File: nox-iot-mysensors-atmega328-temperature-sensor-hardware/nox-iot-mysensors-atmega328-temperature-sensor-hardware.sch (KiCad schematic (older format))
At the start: 14 parts, among them J1 Conn_01x02, J2 FTDI232, U1 ATmega328P-PU, U2 DHT11, U3 NRF24L01+, U5 LM317, Y1 16 MHZ

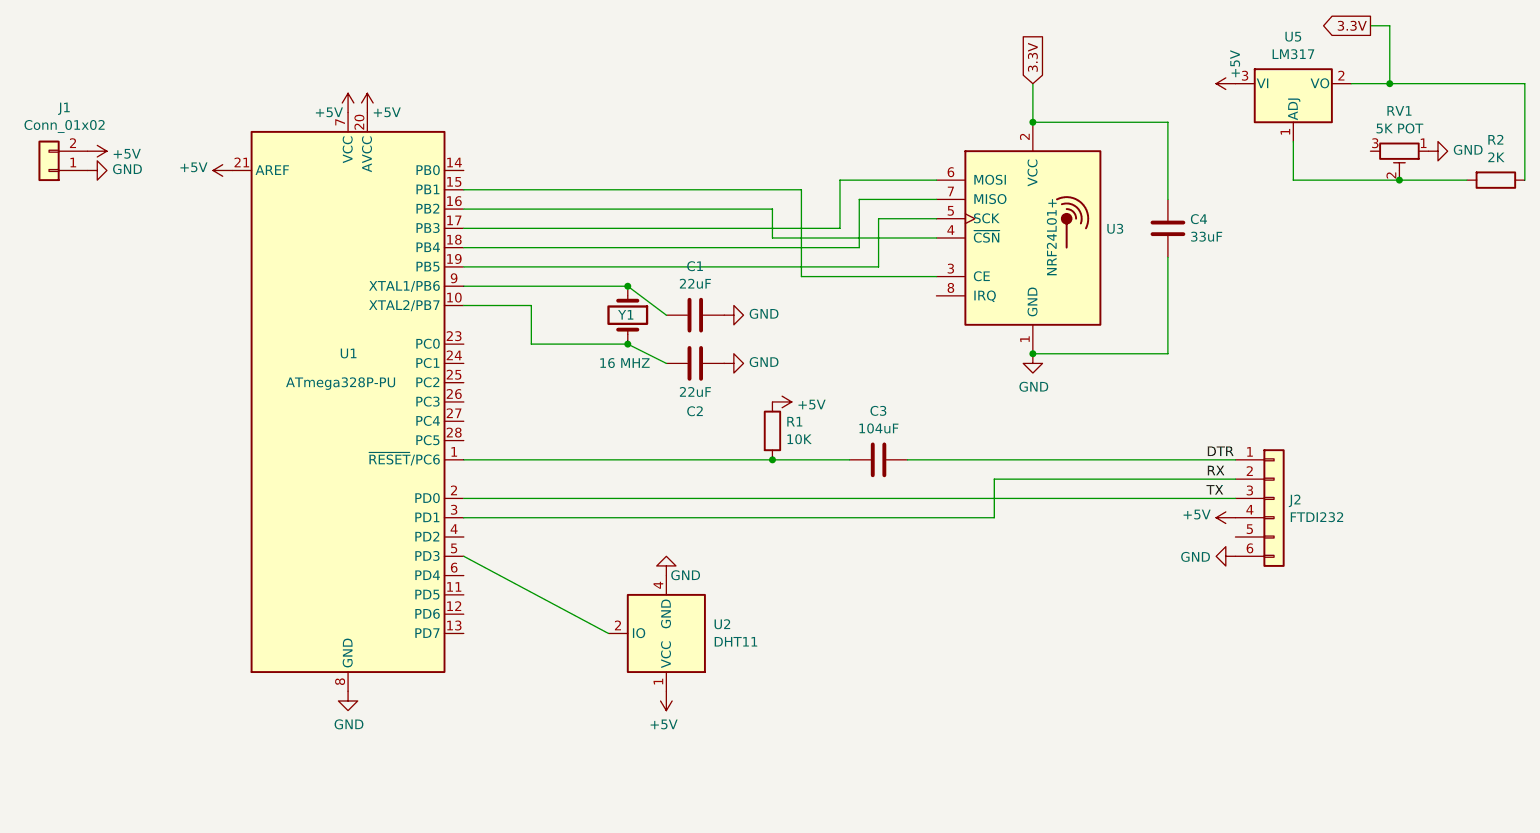
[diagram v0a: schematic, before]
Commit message: aht10 sensor instead of dht11 and 3.3v boost
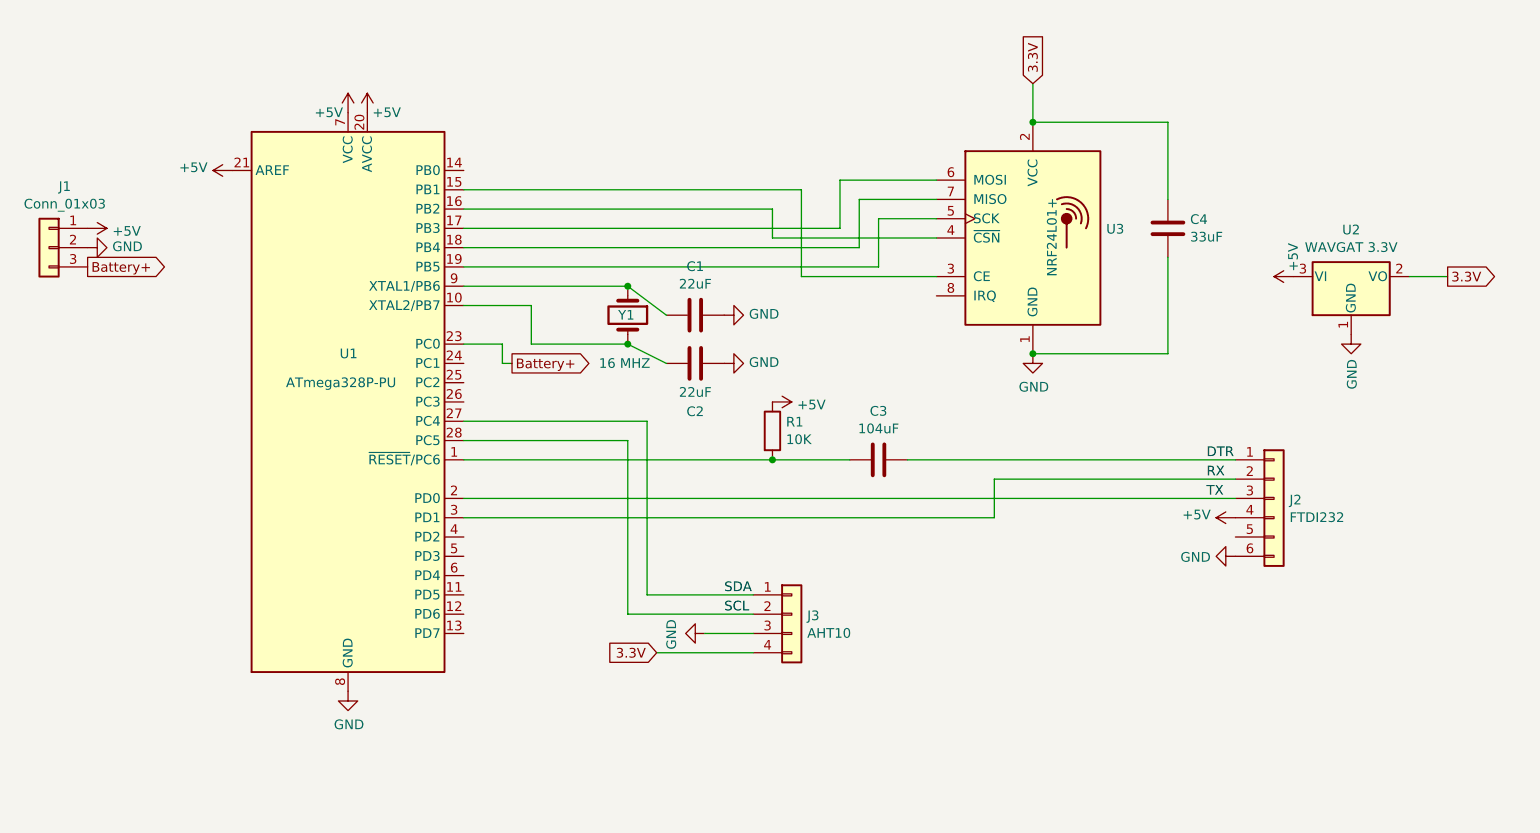
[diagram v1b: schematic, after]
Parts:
- removed J1: Conn_01x02, Connector_JST:JST_XH_B2B-XH-A_1x02_P2.50mm_Vertical, symbol Connector_Generic:Conn_01x02
- removed R2: 2K, Resistor_THT:R_Axial_DIN0204_L3.6mm_D1.6mm_P5.08mm_Horizontal, symbol Device:R
- removed RV1: 5K POT, Potentiometer_THT:Potentiometer_Bourns_3296W_Vertical, symbol Device:R_POT_TRIM
- removed U2: DHT11, Sensor:Aosong_DHT11_5.5x12.0_P2.54mm, symbol Sensor:DHT11
- removed U5: LM317, Package_TO_SOT_THT:TO-220-3_Vertical, symbol Regulator_Linear:LM317_3PinPackage
- added J1: Conn_01x03, Connector_JST:JST_EH_B3B-EH-A_1x03_P2.50mm_Vertical, symbol Connector_Generic:Conn_01x03
- added J3: AHT10, Connector_PinSocket_2.54mm:PinSocket_1x04_P2.54mm_Vertical, symbol Connector_Generic:Conn_01x04
- added U2: WAVGAT 3.3V, Connector_PinSocket_2.54mm:PinSocket_1x03_P2.54mm_Vertical, symbol Regulator_Linear:LM1117-3.3
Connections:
- net +5V: now also J1.1 (Pin_1), U2.3 (VI)
- net 3.3V: now also J3.4 (Pin_4), U2.2 (VO)
- net GND: now also J1.2 (Pin_2), J3.3 (Pin_3), U2.1 (GND)
- net Battery+: now reaches U1.23 (PC0)
- net Battery+: now also J1.3 (Pin_3)
- net SDA: now reaches U1.27 (PC4)
- net SDA: now also J3.1 (Pin_1)
- net SCL: now reaches U1.28 (PC5)
- net SCL: now also J3.2 (Pin_2)
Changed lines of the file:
@@
 Connection ~ 6950 2300
-$Comp
-L power:GND #PWR0104
-U 1 1 5E1E784E
-P 5050 3450
-F 0 "#PWR0104" H 5050 3200 50  0001 C CNN
-F 1 "GND" H 4950 3450 50  0000 C CNN
-F 2 "" H 5050 3450 50  0001 C CNN
-F 3 "" H 5050 3450 50  0001 C CNN
-	1    5050 3450
-	-1   0    0    1
-$EndComp
-$Comp
-L Sensor:DHT11 U2
-U 1 1 5E1B3C29
-P 5050 3750
-F 0 "U2" H 4806 3704 50  0000 R CNN
-F 1 "DHT11" H 4806 3795 50  0000 R CNN
-F 2 "Sensor:Aosong_DHT11_5.5x12.0_P2.54mm" H 5050 3350 50  0001 C CNN
-F 3 "http://akizukidenshi.com/download/ds/aosong/DHT11.pdf" H 5200 4000 50  0001 C CNN
-	1    5050 3750
-	-1   0    0    1
-$EndComp
-Wire Wire Line
-	4000 3350 4750 3750
 $Comp
 L power:GND #PWR0105
@@
 $EndComp
 $Comp
-L Connector_Generic:Conn_01x02 J1
-U 1 1 5E1F447E
-P 1850 1350
-F 0 "J1" H 1768 1025 50  0000 C CNN
-F 1 "Conn_01x02" H 1768 1116 50  0000 C CNN
-F 2 "Connector_JST:JST_XH_B2B-XH-A_1x02_P2.50mm_Vertical" H 1850 1350 50  0001 C CNN
-F 3 "~" H 1850 1350 50  0001 C CNN
-	1    1850 1350
-	-1   0    0    1
-$EndComp
-$Comp
-L power:GND #PWR0106
-U 1 1 5E1F540D
-P 2050 1350
-F 0 "#PWR0106" H 2050 1100 50  0001 C CNN
-F 1 "GND" V 2055 1222 50  0000 R CNN
-F 2 "" H 2050 1350 50  0001 C CNN
-F 3 "" H 2050 1350 50  0001 C CNN
-	1    2050 1350
-	0    -1   -1   0
-$EndComp
-$Comp
-L power:+5V #PWR0107
-U 1 1 5E1F59FF
-P 2050 1250
-F 0 "#PWR0107" H 2050 1100 50  0001 C CNN
-F 1 "+5V" V 2065 1378 50  0000 L CNN
-F 2 "" H 2050 1250 50  0001 C CNN
-F 3 "" H 2050 1250 50  0001 C CNN
-	1    2050 1250
-	0    1    1    0
-$EndComp
-$Comp
 L power:+5V #PWR0108
 U 1 1 5E1F682D
@@
 $EndComp
 $Comp
-L power:+5V #PWR0110
-U 1 1 5E1FC63D
-P 5050 4050
-F 0 "#PWR0110" H 5050 3900 50  0001 C CNN
-F 1 "+5V" H 5065 4223 50  0000 C CNN
-F 2 "" H 5050 4050 50  0001 C CNN
-F 3 "" H 5050 4050 50  0001 C CNN
-	1    5050 4050
-	-1   0    0    1
-$EndComp
-$Comp
 L power:+5V #PWR0111
 U 1 1 5E1FCC86
@@
 Text Label 7850 3050 0    50   ~ 0
 TX
-$Comp
-L Device:R_POT_TRIM RV1
-U 1 1 5E2569EA
-P 8850 1250
-F 0 "RV1" V 8643 1250 50  0000 C CNN
-F 1 "5K POT" V 8734 1250 50  0000 C CNN
-F 2 "Potentiometer_THT:Potentiometer_Bourns_3296W_Vertical" H 8850 1250 50  0001 C CNN
-F 3 "~" H 8850 1250 50  0001 C CNN
-	1    8850 1250
-	0    1    1    0
-$EndComp
-$Comp
-L power:+5V #PWR0115
-U 1 1 5E25E144
-P 8000 900
-F 0 "#PWR0115" H 8000 750 50  0001 C CNN
-F 1 "+5V" H 8100 900 50  0000 C CNN
-F 2 "" H 8000 900 50  0001 C CNN
-F 3 "" H 8000 900 50  0001 C CNN
-	1    8000 900
-	0    -1   -1   0
-$EndComp
-$Comp
-L Device:R R2
-U 1 1 5E25F822
-P 9350 1400
-F 0 "R2" V 9143 1400 50  0000 C CNN
-F 1 "2K" V 9234 1400 50  0000 C CNN
-F 2 "Resistor_THT:R_Axial_DIN0204_L3.6mm_D1.6mm_P5.08mm_Horizontal" V 9280 1400 50  0001 C CNN
-F 3 "~" H 9350 1400 50  0001 C CNN
-	1    9350 1400
-	0    1    1    0
-$EndComp
-Wire Wire Line
-	8300 1200 8300 1400
-Wire Wire Line
-	8300 1400 8850 1400
-$Comp
-L power:GND #PWR0116
-U 1 1 5E260C49
-P 9000 1250
-F 0 "#PWR0116" H 9000 1000 50  0001 C CNN
-F 1 "GND" V 9005 1122 50  0000 R CNN
-F 2 "" H 9000 1250 50  0001 C CNN
-F 3 "" H 9000 1250 50  0001 C CNN
-	1    9000 1250
-	0    -1   -1   0
-$EndComp
-Wire Wire Line
-	8850 1400 9200 1400
-Connection ~ 8850 1400
-Wire Wire Line
-	9500 1400 9500 900
-Wire Wire Line
-	9500 900  8800 900
-Wire Wire Line
-	8800 900  8800 600
-Connection ~ 8800 900
-Wire Wire Line
-	8800 900  8600 900
-Text GLabel 8700 600  0    50   Output ~ 0
-3.3V
-Wire Wire Line
-	8800 600  8700 600
 Text GLabel 6950 900  1    50   Input ~ 0
 3.3V
@@
 	6950 900  6950 1100
 $Comp
-L Regulator_Linear:LM317_3PinPackage U5
-U 1 1 5E283E2A
-P 8300 900
-F 0 "U5" H 8300 1142 50  0000 C CNN
-F 1 "LM317" H 8300 1051 50  0000 C CNN
-F 2 "Package_TO_SOT_THT:TO-220-3_Vertical" H 8300 1150 50  0001 C CIN
-F 3 "http://www.ti.com/lit/ds/symlink/lm317.pdf" H 8300 900 50  0001 C CNN
-	1    8300 900
-	1    0    0    -1
-$EndComp
+L Regulator_Linear:LM1117-3.3 U2
+U 1 1 5E2DE152
+P 8600 1900
+F 0 "U2" H 8600 2142 50  0000 C CNN
+F 1 "WAVGAT 3.3V" H 8600 2051 50  0000 C CNN
+F 2 "Connector_PinSocket_2.54mm:PinSocket_1x03_P2.54mm_Vertical" H 8600 1900 50  0001 C CNN
+F 3 "http://www.ti.com/lit/ds/symlink/lm1117.pdf" H 8600 1900 50  0001 C CNN
+	1    8600 1900
+	1    0    0    -1
+$EndComp
+$Comp
+L power:+5V #PWR02
+U 1 1 5E2DFBC7
+P 8300 1900
+F 0 "#PWR02" H 8300 1750 50  0001 C CNN
+F 1 "+5V" H 8400 1900 50  0000 C CNN
+F 2 "" H 8300 1900 50  0001 C CNN
+F 3 "" H 8300 1900 50  0001 C CNN
+	1    8300 1900
+	0    -1   -1   0
+$EndComp
+$Comp
+L power:GND #PWR03
+U 1 1 5E2E0195
+P 8600 2200
+F 0 "#PWR03" H 8600 1950 50  0001 C CNN
+F 1 "GND" V 8605 2072 50  0000 R CNN
+F 2 "" H 8600 2200 50  0001 C CNN
+F 3 "" H 8600 2200 50  0001 C CNN
+	1    8600 2200
+	1    0    0    -1
+$EndComp
+Text GLabel 9100 1900 2    50   Output ~ 0
+3.3V
+Wire Wire Line
+	8900 1900 9100 1900
+Text GLabel 5000 3850 0    50   Input ~ 0
+3.3V
+Wire Wire Line
+	5500 3850 5000 3850
+$Comp
+L power:GND #PWR01
+U 1 1 5E2F2798
+P 5250 3750
+F 0 "#PWR01" H 5250 3500 50  0001 C CNN
+F 1 "GND" H 5255 3577 50  0000 C CNN
+F 2 "" H 5250 3750 50  0001 C CNN
+F 3 "" H 5250 3750 50  0001 C CNN
+	1    5250 3750
+	0    1    1    0
+$EndComp
+Wire Wire Line
+	5250 3750 5500 3750
+Wire Wire Line
+	4000 2750 4850 2750
+Wire Wire Line
+	4850 2750 4850 3650
+Wire Wire Line
+	4850 3650 5500 3650
+Wire Wire Line
+	4000 2650 4950 2650
+Wire Wire Line
+	4950 2650 4950 3550
+Wire Wire Line
+	4950 3550 5500 3550
+Text Label 5350 3550 0    50   ~ 0
+SDA
+Text Label 5350 3650 0    50   ~ 0
+SCL
+$Comp
+L Connector_Generic:Conn_01x03 J1
+U 1 1 5E2E1CFC
+P 1850 1750
+F 0 "J1" H 1768 2067 50  0000 C CNN
+F 1 "Conn_01x03" H 1768 1976 50  0000 C CNN
+F 2 "Connector_JST:JST_EH_B3B-EH-A_1x03_P2.50mm_Vertical" H 1850 1750 50  0001 C CNN
+F 3 "~" H 1850 1750 50  0001 C CNN
+	1    1850 1750
+	-1   0    0    -1
+$EndComp
+$Comp
+L power:+5V #PWR04
+U 1 1 5E2E3230
+P 2050 1650
+F 0 "#PWR04" H 2050 1500 50  0001 C CNN
+F 1 "+5V" V 2065 1778 50  0000 L CNN
+F 2 "" H 2050 1650 50  0001 C CNN
+F 3 "" H 2050 1650 50  0001 C CNN
+	1    2050 1650
+	0    1    1    0
+$EndComp
+$Comp
+L power:GND #PWR05
+U 1 1 5E2E3606
+P 2050 1750
+F 0 "#PWR05" H 2050 1500 50  0001 C CNN
+F 1 "GND" V 2055 1622 50  0000 R CNN
+F 2 "" H 2050 1750 50  0001 C CNN
+F 3 "" H 2050 1750 50  0001 C CNN
+	1    2050 1750
+	0    -1   -1   0
+$EndComp
+Text GLabel 2050 1850 2    50   Output ~ 0
+Battery+
+Text GLabel 4250 2350 2    50   Output ~ 0
+Battery+
+Wire Wire Line
+	4250 2350 4200 2350
+Wire Wire Line
+	4200 2350 4200 2250
+Wire Wire Line
+	4200 2250 4000 2250
+$Comp
+L Connector_Generic:Conn_01x04 J3
+U 1 1 5E2EC327
+P 5700 3650
+F 0 "J3" H 5780 3642 50  0000 L CNN
+F 1 "AHT10" H 5780 3551 50  0000 L CNN
+F 2 "Connector_PinSocket_2.54mm:PinSocket_1x04_P2.54mm_Vertical" H 5700 3650 50  0001 C CNN
+F 3 "~" H 5700 3650 50  0001 C CNN
+	1    5700 3650
+	1    0    0    -1
+$EndComp
